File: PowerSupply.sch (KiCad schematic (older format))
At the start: 33 parts

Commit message: start placement
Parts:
- removed C?: 100n, Capacitor_SMD:C_0603_1608Metric, symbol AR2ISS:C
- removed D?: BZX84Cxx, Diode_SMD:D_SOT-23_ANK, symbol Diode:BZX84Cxx
- removed J?: Conn_01x04, AR2ISS:250-204, symbol Connector_Generic:Conn_01x04
- removed R?: 33k, Resistor_SMD:R_0603_1608Metric, symbol AR2ISS:R
- removed R?: 3k, Resistor_SMD:R_0603_1608Metric, symbol AR2ISS:R
- added D20: D_Zener, symbol Device:D_Zener
- added D21: D_TVS, symbol Device:D_TVS
- added Q7: PMN48XP, Package_SO:TSOP-6_1.65x3.05mm_P0.95mm, symbol Transistor_FET:PMN48XP
- added R42: R, symbol AR2ISS:R
- gave numbers to parts that had none: 28
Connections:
- net labels removed: +24V, ADC24V
- wire segments 114 -> 104
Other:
- note added: "PMN100EPAX"
- moved on the sheet: C50, C51, C52, C53, C55, C56, C57, C58, C59, C60, C61, C62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

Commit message: placement
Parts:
- R42: value R -> 470
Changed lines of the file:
@@
 $Descr A4 11693 8268
 encoding utf-8
-Sheet 13 21
+Sheet 10 22
 Title ""
 Date ""
@@
 P 2100 2650
 F 0 "R42" H 2170 2696 50  0000 L CNN
-F 1 "R" H 2170 2605 50  0000 L CNN
+F 1 "470" H 2170 2605 50  0000 L CNN
 F 2 "" V 2030 2650 50  0001 C CNN
 F 3 "~" H 2100 2650 50  0001 C CNN

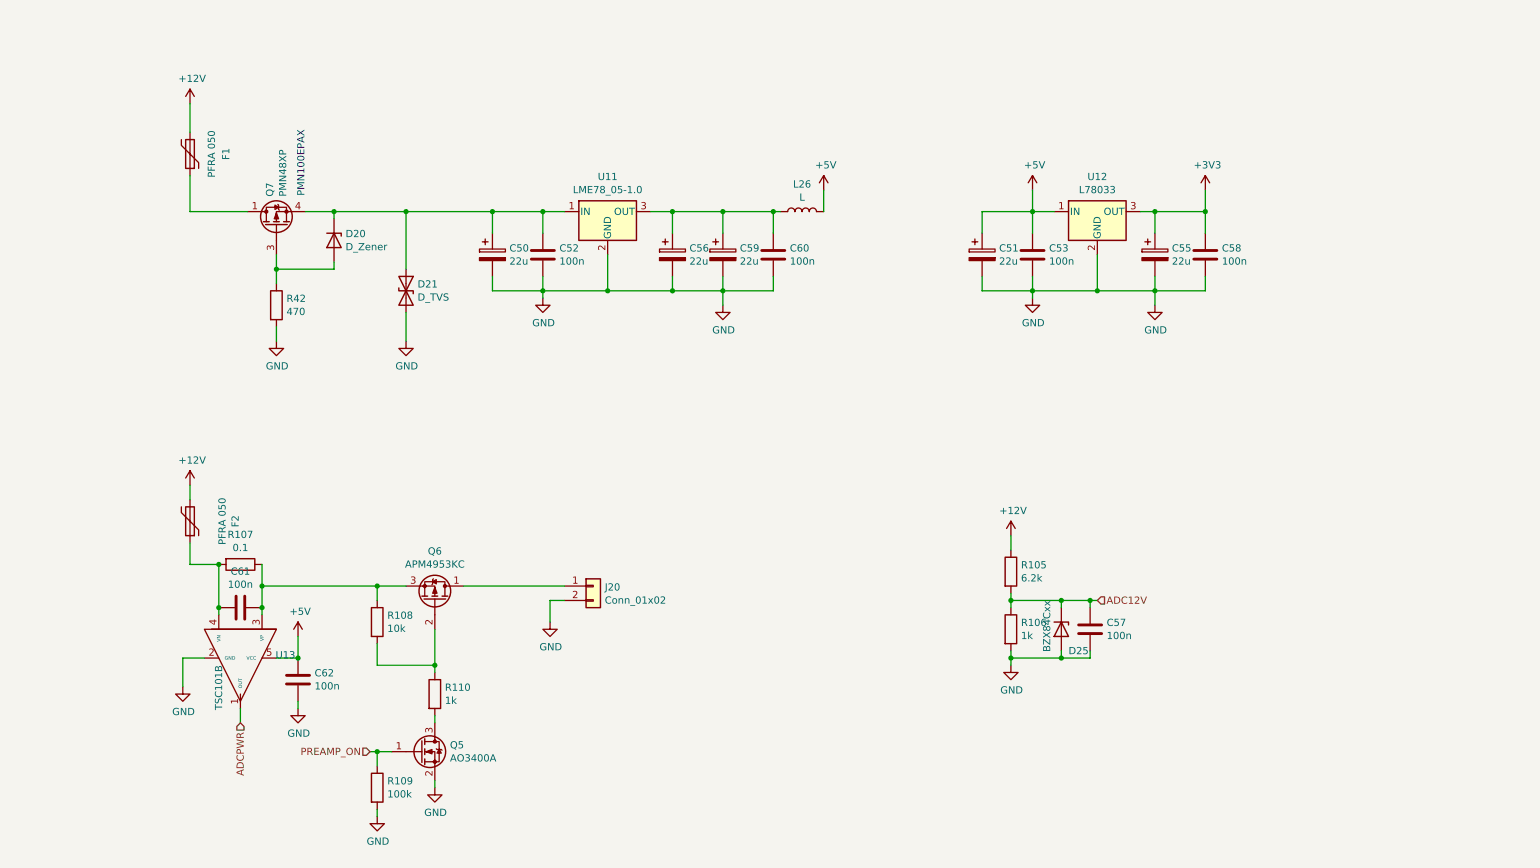
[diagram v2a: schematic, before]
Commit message: add TLE5602
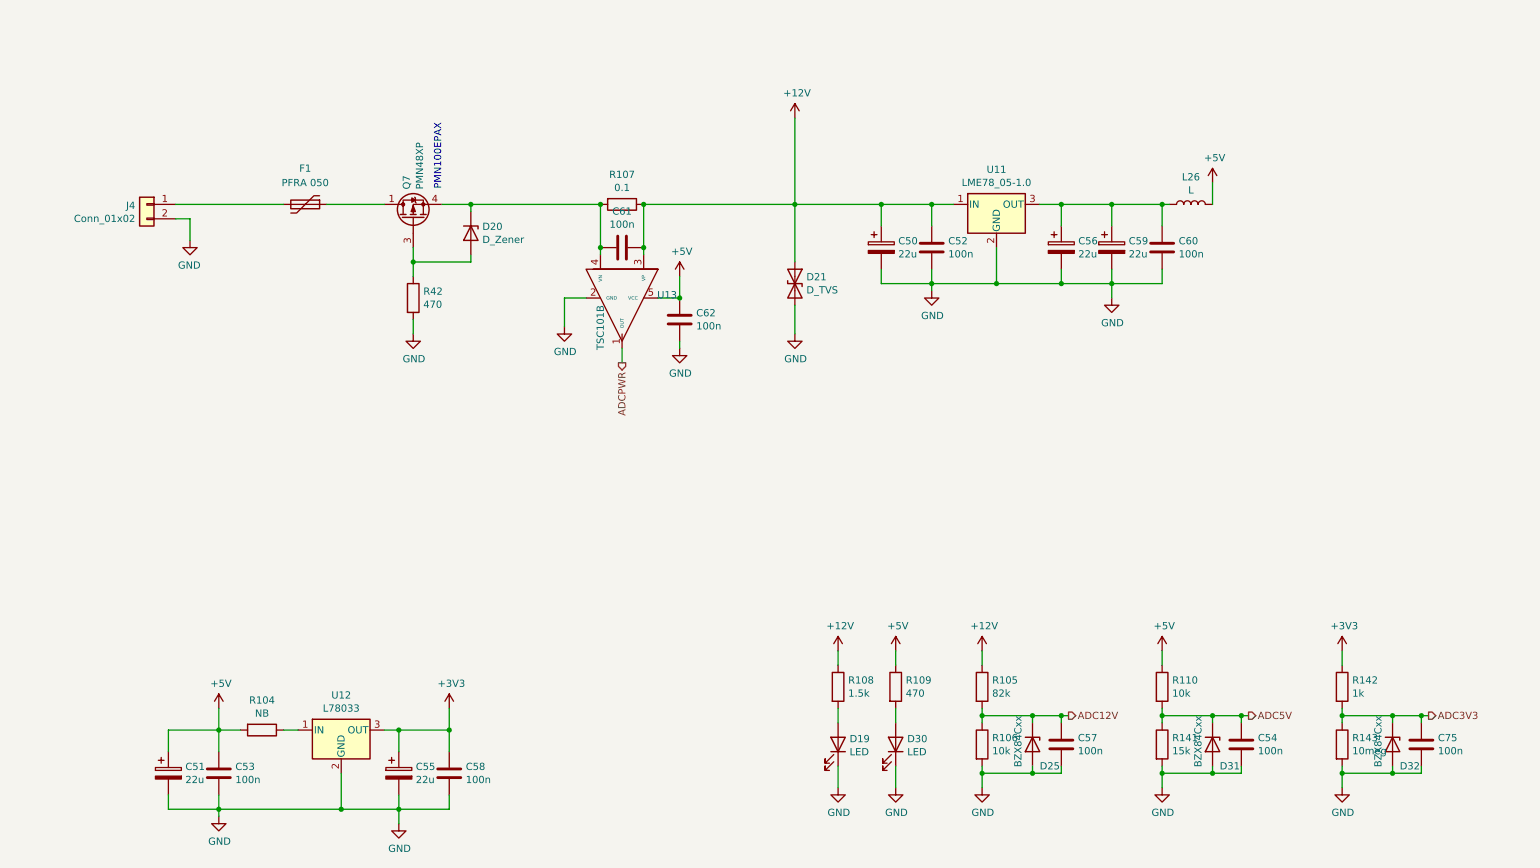
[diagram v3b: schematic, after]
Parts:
- removed F2: PFRA 050, Fuse:Fuse_BelFuse_0ZRE0005FF_L8.3mm_W3.8mm, symbol Device:Polyfuse
- removed J20: Conn_01x02, stmbl:RM3.5_1x2, symbol Connector_Generic:Conn_01x02
- removed Q5: AO3400A, Package_TO_SOT_SMD:SOT-23, symbol Transistor_FET:AO3400A
- removed Q6: APM4953KC, Package_SO:SO-8_5.3x6.2mm_P1.27mm, symbol Device:Q_PMOS_DGS
- added C54, C75: 100n, Capacitor_SMD:C_0603_1608Metric, symbol AR2ISS:C
- added D19, D30: LED, LED_SMD:LED_0603_1608Metric, symbol Device:LED
- added D31, D32: BZX84Cxx, Diode_SMD:D_SOT-23_ANK, symbol Diode:BZX84Cxx
- added J4: Conn_01x02, AR2ISS:250-202, symbol Connector_Generic:Conn_01x02
- added R104: NB, Resistor_SMD:R_0603_1608Metric, symbol AR2ISS:R
- added R141: 15k, Resistor_SMD:R_0603_1608Metric, symbol AR2ISS:R
- added R142: 1k, Resistor_SMD:R_0603_1608Metric, symbol AR2ISS:R
- added R143: 10meg, Resistor_SMD:R_0603_1608Metric, symbol AR2ISS:R
- D20: footprint (none) -> Diode_SMD:D_SOD-123
- D21: footprint (none) -> Diode_SMD:D_SMA-SMB_Universal_Handsoldering
- R105: value 6.2k -> 82k
- R106, R110: value 1k -> 10k
- R108: value 10k -> 1.5k
- R109: value 100k -> 470
- R42: footprint (none) -> Resistor_SMD:R_0603_1608Metric
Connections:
- net PREAMP_ON is gone; now on net +5V: R109.1
- net +12V: now also C50.1, C52.1, C61.2, D21.1 (A1), R107.1, R108.1, U11.1 (IN), U13.3 (VP); no longer F1.2
- net +3V3: now also R142.1
- net +5V: now also R110.1, R104.2; no longer U12.1 (IN)
- net GND: now also C54.2, C75.2, D19.1 (K), D30.1 (K), D31.2 (A), D32.2 (A), J4.2 (Pin_2), R141.2, R143.2; no longer R109.2
- net at C61.1, R107.2, U13.4 (VN): now also D20.1 (K), Q7.4 (S)
- net at R108.2: now also D19.2 (A); no longer R110.1
- net ADC5V: now reaches R110.2
- net ADC5V: now also C54.1, D31.1 (K), R141.1
- new net: R104.1, U12.1 (IN)
- new net: F1.2, J4.1 (Pin_1)
- new net: D30.2 (A), R109.2
- new net ADC3V3: C75.1, D32.1 (K), R142.2, R143.1
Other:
- moved on the sheet: C50, C51, C52, C53, C55, C56, C57, C58, C59, C60, C61, C62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

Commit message: routing
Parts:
- D25, D31, D32: value BZX84Cxx -> BZX84C3V6,215
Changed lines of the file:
@@
 P 7350 5700
 F 0 "D25" V 7500 5750 50  0000 L CNN
-F 1 "BZX84Cxx" H 7150 5600 50  0000 L CNN
+F 1 "BZX84C3V6,215" H 7150 5600 50  0000 L CNN
 F 2 "Diode_SMD:D_SOT-23_ANK" H 7350 5525 50  0001 C CNN
 F 3 "https://diotec.com/tl_files/diotec/files/pdf/datasheets/bzx84c2v4.pdf" H 7350 5700 50  0001 C CNN
@@
 P 8600 5700
 F 0 "D31" V 8750 5750 50  0000 L CNN
-F 1 "BZX84Cxx" H 8400 5600 50  0000 L CNN
+F 1 "BZX84C3V6,215" H 8400 5600 50  0000 L CNN
 F 2 "Diode_SMD:D_SOT-23_ANK" H 8600 5525 50  0001 C CNN
 F 3 "https://diotec.com/tl_files/diotec/files/pdf/datasheets/bzx84c2v4.pdf" H 8600 5700 50  0001 C CNN
@@
 P 9850 5700
 F 0 "D32" V 10000 5750 50  0000 L CNN
-F 1 "BZX84Cxx" H 9650 5600 50  0000 L CNN
+F 1 "BZX84C3V6,215" H 9650 5600 50  0000 L CNN
 F 2 "Diode_SMD:D_SOT-23_ANK" H 9850 5525 50  0001 C CNN
 F 3 "https://diotec.com/tl_files/diotec/files/pdf/datasheets/bzx84c2v4.pdf" H 9850 5700 50  0001 C CNN

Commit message: ready for jlc
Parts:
- D19, D30: value LED -> LED_G
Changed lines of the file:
@@
 $Descr A4 11693 8268
 encoding utf-8
-Sheet 10 22
+Sheet 9 22
 Title ""
 Date ""
@@
 AR Path="/60A2EE09/60B4A275" Ref="D19"  Part="1"
 F 0 "D19" V 6039 5780 50  0000 L CNN
-F 1 "LED" V 5948 5780 50  0000 L CNN
+F 1 "LED_G" V 5948 5780 50  0000 L CNN
 F 2 "LED_SMD:LED_0603_1608Metric" H 6000 5700 50  0001 C CNN
 F 3 "~" H 6000 5700 50  0001 C CNN
@@
 AR Path="/60A2EE09/60B5ADA4" Ref="D30"  Part="1"
 F 0 "D30" V 6439 5780 50  0000 L CNN
-F 1 "LED" V 6348 5780 50  0000 L CNN
+F 1 "LED_G" V 6348 5780 50  0000 L CNN
 F 2 "LED_SMD:LED_0603_1608Metric" H 6400 5700 50  0001 C CNN
 F 3 "~" H 6400 5700 50  0001 C CNN
